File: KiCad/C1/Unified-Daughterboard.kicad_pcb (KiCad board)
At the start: 2 copper layers, 18 x 16.5 mm, 8 parts, among them J1 HRO-TYPE-C-31-M-12, J2 Conn_01x04

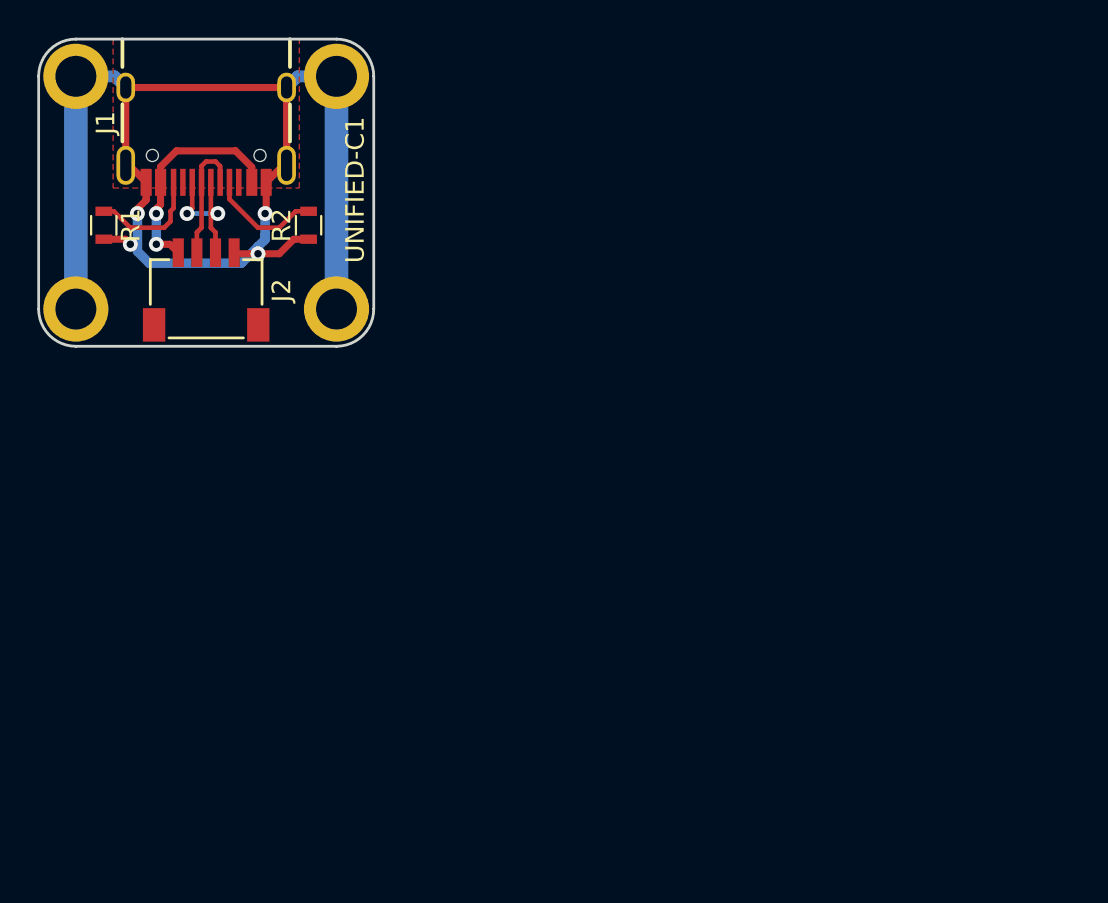
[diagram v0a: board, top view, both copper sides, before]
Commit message: Improved grounding and shielding
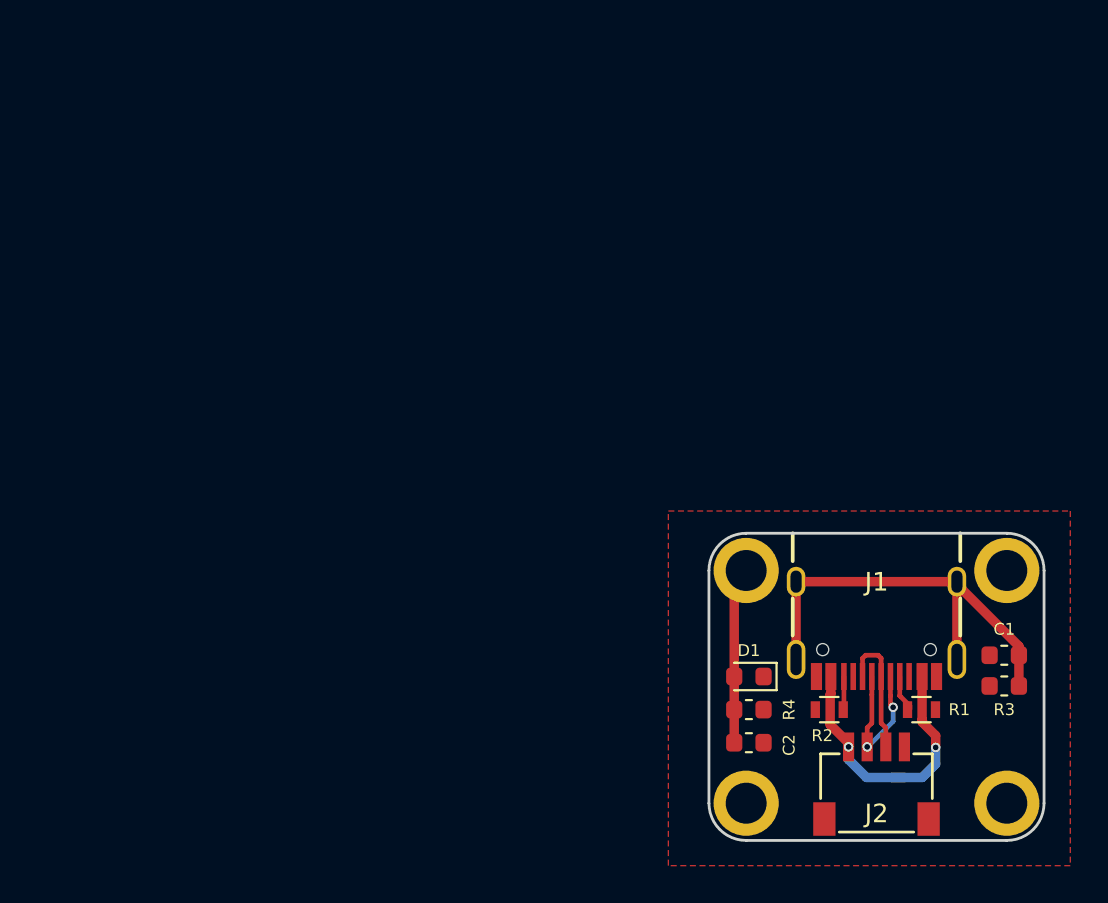
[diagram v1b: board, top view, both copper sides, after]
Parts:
- added C1: 10n, Capacitor_SMD:C_0603_1608Metric, F.Cu at (81.9, 63.1)
- added C2: 10n, Capacitor_SMD:C_0603_1608Metric, F.Cu at (68.2, 67.8)
- added D1: ESD5451XZ-2/TR, Diode_SMD:D_0603_1608Metric, F.Cu at (68.2, 64.2)
- added R3: 1M, Resistor_SMD:R_0603_1608Metric, F.Cu at (81.9, 64.7)
- added R4: 1M, Resistor_SMD:R_0603_1608Metric, F.Cu at (68.2, 66.0)
- J2: value Conn_01x04 -> JST-SR-4
- moved R1 51.0 mm to (77.4, 66.0), turned to 0 degrees
- moved J2 44.7 mm to (75.0, 72.8)
- moved MH3 44.7 mm to (68.0, 71.0)
- moved MH4 44.7 mm to (82.0, 71.0)
- moved J1 44.7 mm to (75.0, 56.5)
- moved MH1 44.7 mm to (68.0, 58.5)
- moved MH2 44.7 mm to (82.0, 58.5)
- moved R2 38.2 mm to (72.5, 66.0), turned to 180 degrees
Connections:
- J1 pad 13: GND -> Net-(C1-Pad1)
- MH1 pad 1: GND -> Net-(C2-Pad1)
- MH2 pad 1: GND -> Net-(MH2-Pad1)
- MH3 pad 1: GND -> Net-(MH3-Pad1)
- MH4 pad 1: GND -> Net-(MH4-Pad1)
- R1 pad 1: Net-(J1-Pad10) -> Net-(J1-Pad4)
- R2 pad 1: Net-(J1-Pad4) -> Net-(J1-Pad10)
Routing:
- net GND: track 72.2 -> 0.00 mm, vias 4 -> 0
- net Net-(C1-Pad1): track 0.00 -> 24.0 mm
- net Net-(C2-Pad1): track 0.00 -> 9.25 mm
- net Net-(J1-Pad10): track 6.25 -> 1.78 mm
- net VCC: track 12.1 -> 16.0 mm
- net Net-(J1-Pad4): track 6.15 -> 2.19 mm
- net D-: track 6.83 -> 8.32 mm, vias 0 -> 2
- net D+: track 7.70 -> 6.98 mm, vias 2 -> 0
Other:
- board text added: "Variant C2"
- board text removed: "UNIFIED-C1"
- board text removed: "Variant C1"
